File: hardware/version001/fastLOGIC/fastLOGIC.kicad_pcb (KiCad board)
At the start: 2 copper layers, 60 x 92 mm, 82 parts, among them J1 AVR-ISP-6, J10 0-5V_ANALOG_IN_A, J11 PRES_SENS_BOTTOM, J12 PRES_SENS_TOP, J13 0-5V_ANALOG_IN_B, J14 RELAY_OUT_B, J15 RELAY_OUT_A, J2 USB_B_Micro, J3 DS18B20, J4 12-24V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

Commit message: hardware chnages minor
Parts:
- removed J2: USB_B_Micro, Connector_USB:USB_Micro-B_Amphenol_10118194_Horizontal
- added J6: USB_B_Mini, Connector_USB:USB_Mini-B_Tensility_54-00023_Vertical, F.Cu at (33.7, 57.0)
- moved C16 1.10 mm to (38.0, 64.4)
- moved C13 1.10 mm to (36.2, 64.6)
- moved H3 0.75 mm to (81.0, 87.8)
- moved H5 0.75 mm to (39.0, 87.8)
- moved C6 0.50 mm to (80.5, 94.0)
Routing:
- net unconnected-(J2-Shield-Pad6): track 11.8 -> 0.00 mm
- net Net-(J6-D+): track 8.10 -> 9.94 mm, vias 2 -> 0
- net Net-(J6-VBUS): track 18.4 -> 19.2 mm, vias 2 -> 1
- net GND: track 15.3 -> 14.6 mm, vias 202 -> 212
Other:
- board text added: "DEBUG USB"

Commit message: latest pcb
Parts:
- U3, U4: footprint Package_DIP:DIP-4_W7.62mm_SMDSocket_SmallPads -> Package_DIP:DIP-4_W8.89mm_SMDSocket_LongPads
- moved C15 2.31 mm to (44.0, 64.1), turned to 180 degrees
- moved C14 2.16 mm to (41.5, 64.6)
- moved R13 0.82 mm to (43.3, 79.7)
- moved R22 0.82 mm to (46.3, 79.7)
- moved R6 0.81 mm to (53.8, 79.7)
- moved R7 0.81 mm to (50.8, 79.7)
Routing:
- net Net-(R6-Pad1): track 2.58 -> 4.72 mm
- net DIG_IN_A: track 34.9 -> 36.9 mm
- net Net-(J9-Pin_2): track 31.3 -> 33.0 mm
- net Net-(R22-Pad1): track 2.80 -> 4.36 mm
- net Net-(J8-Pin_2): track 14.8 -> 16.3 mm
- net +5V: track 276.5 -> 277.5 mm
- net GND: vias 212 -> 211

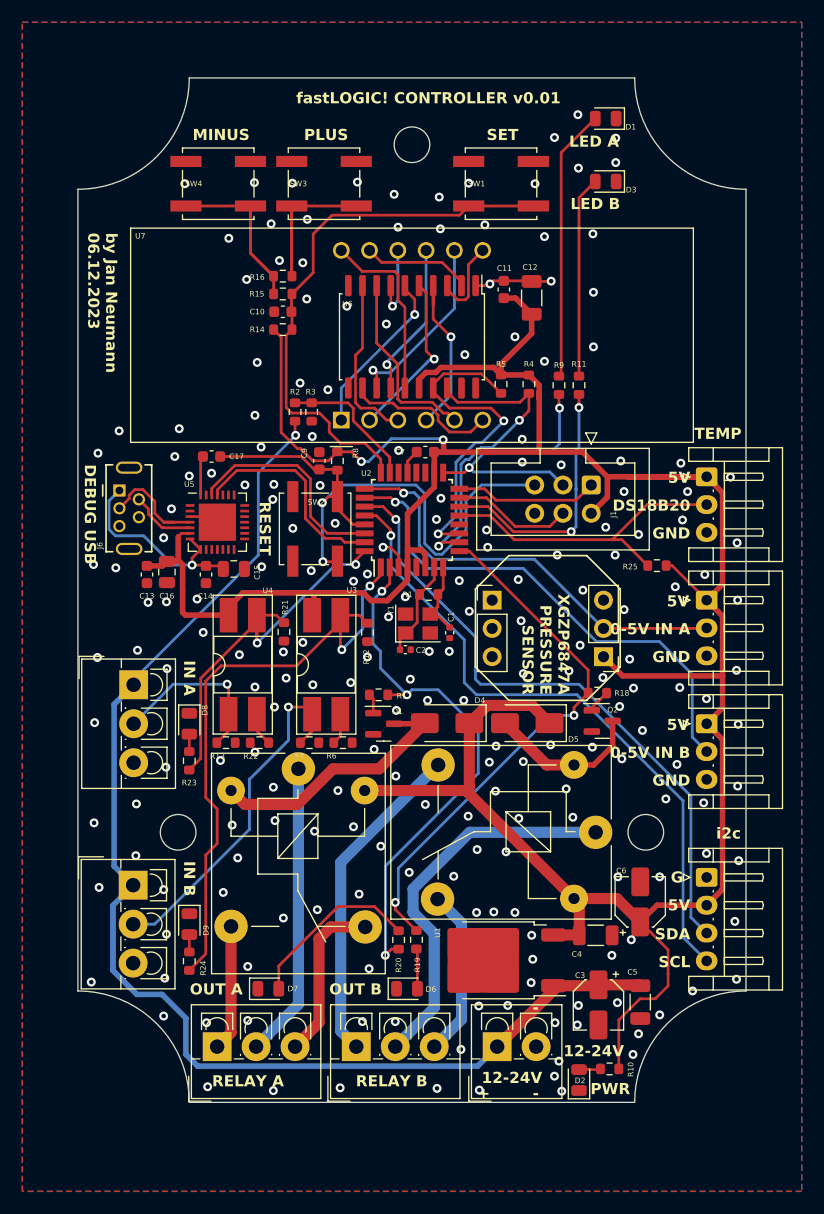
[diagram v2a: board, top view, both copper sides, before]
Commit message: changed holes, vias and markings
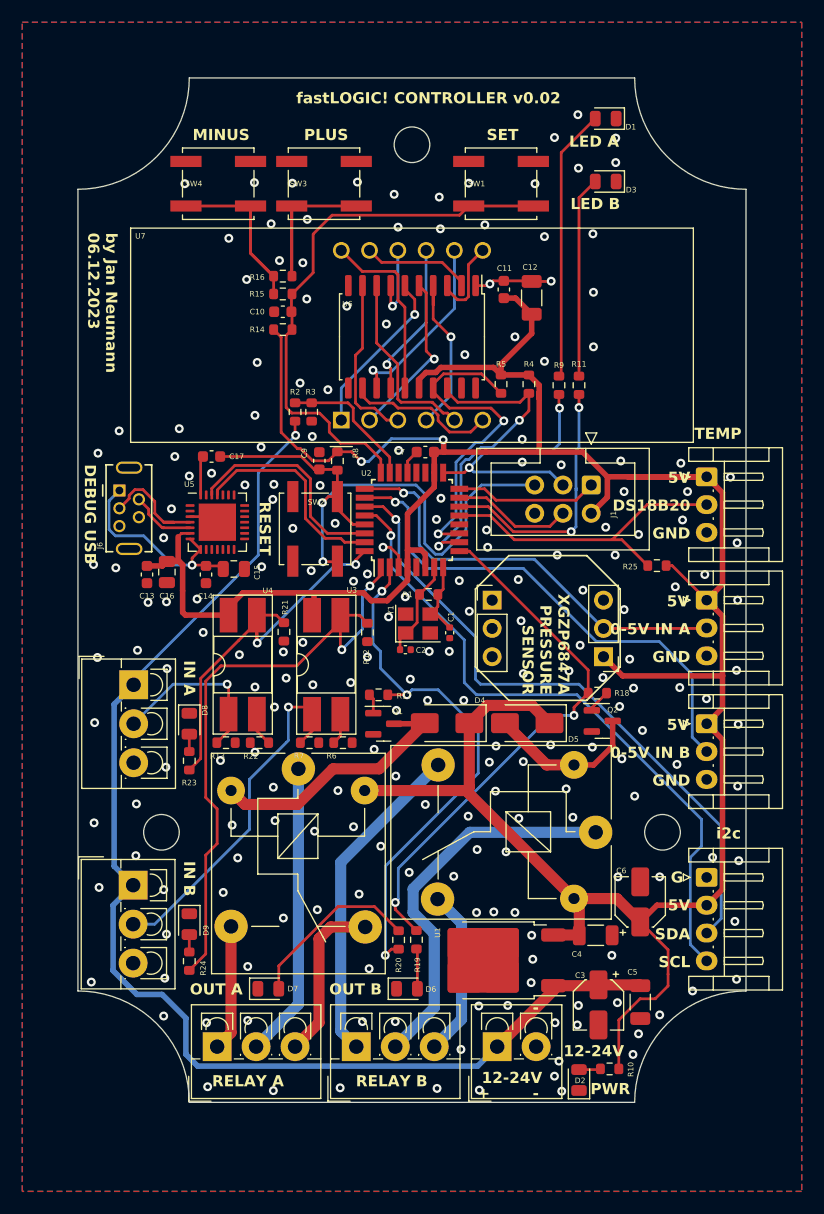
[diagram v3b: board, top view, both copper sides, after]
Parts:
- moved H3 1.50 mm to (82.5, 87.8)
- moved H5 1.50 mm to (37.5, 87.8)
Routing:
- net SDA: track 57.2 -> 58.3 mm
- net SCL: track 58.6 -> 59.5 mm
- net GND: vias 211 -> 209
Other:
- board text added: "fastLOGIC! CONTROLLER v0.02"
- board text removed: "fastLOGIC! CONTROLLER v0.01"

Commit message: minor pcb changes, image
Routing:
- net Net-(D7-A): track 15.9 -> 19.8 mm
- net +5V: track 277.5 -> 281.3 mm
- net GND: track 14.6 -> 16.8 mm, vias 209 -> 226
- net Net-(J14-Pin_3): track 15.2 -> 13.4 mm
- net D_OUT_A: track 48.3 -> 49.5 mm
- net Net-(D4-A): track 23.7 -> 24.7 mm
- net D_OUT_B: track 48.6 -> 49.5 mm
- net DIG_IN_B: track 55.9 -> 55.1 mm
- net Net-(J14-Pin_1): track 29.5 -> 30.2 mm
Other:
- board text added: "by Jan Neumann 04.01.2024"
- board text removed: "by Jan Neumann 06.12.2023"
